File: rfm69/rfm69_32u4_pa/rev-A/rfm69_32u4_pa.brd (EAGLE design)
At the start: 69.8 x 69.8 mm, 125 parts, among them IC1 ATMEGA32U4-AU, IC2 74HC04D, IC3 MCP9700, SW1 HMC284AMS8G, SW1A TPSQTP10SQ, SW1B TPSQTP10SQ, SW2 HMC574AMS8E, SW2A TPSQTP10SQ, SW2B TPSQTP10SQ, Y1 8MHz

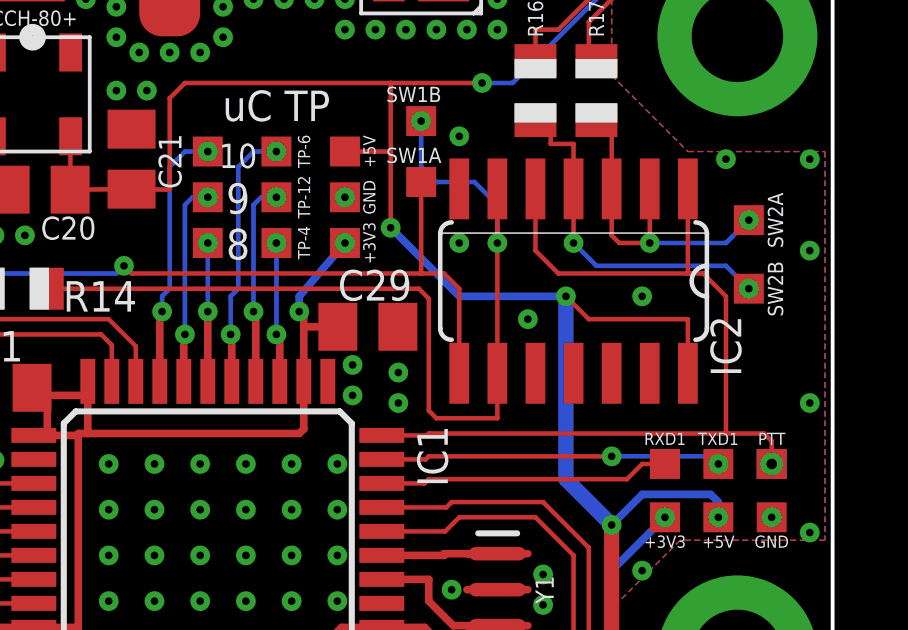
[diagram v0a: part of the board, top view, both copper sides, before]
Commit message: Changed PTT pin from physical pin 22 to physical pin 25 which is mapped to arduino digital pin 4.  This was done because there is no mapping of physical pin 22 to an arduino digital pin for the feather32u4.
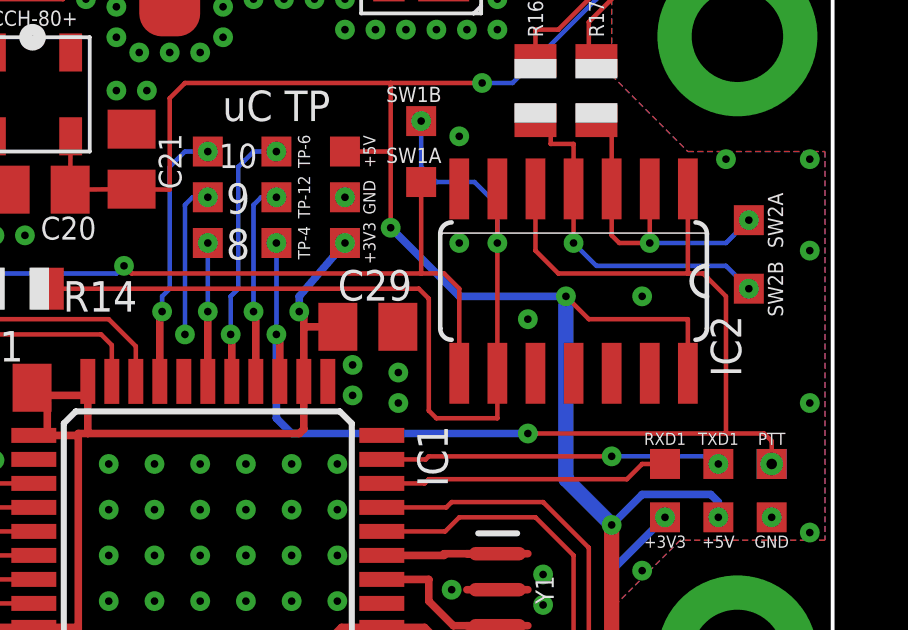
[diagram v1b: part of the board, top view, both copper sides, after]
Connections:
- removed net 22_TXRX_PTT: IC1.22, IC2.1, IC2.5, PTT.TP, PTT2.TP
- removed net 4: IC1.25, TP-4.TP
- new net 4_TXRX_PTT: IC1.25, IC2.1, IC2.5, PTT.TP, PTT2.TP, TP-4.TP
- new net NA: IC1.22
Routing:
- net 4_TXRX_PTT: track 0.00 -> 41.6 mm, vias 0 -> 4
- net 22_TXRX_PTT: track 30.3 -> 0.00 mm, vias 1 -> 0
- net 4: track 4.66 -> 0.00 mm, vias 2 -> 0
- net 9: track 6.77 -> 5.24 mm
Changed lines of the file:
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@@
 </signal>
 <signal name="9">
-<contactref element="IC1" pad="29"/>
 <contactref element="9" pad="TP"/>
 <via x="48.26" y="35.306" extent="1-16" drill="0.254"/>
-<wire x1="48.222" y1="33.74" x2="48.222" y2="35.268" width="0.254" layer="1"/>
 <wire x1="48.222" y1="35.268" x2="48.26" y2="35.306" width="0.254" layer="1"/>
 <via x="49.022" y="39.878" extent="1-16" drill="0.254"/>
@@
 <wire x1="48.26" y1="39.624" x2="48.514" y2="39.878" width="0.1524" layer="16"/>
 <wire x1="48.514" y1="39.878" x2="49.022" y2="39.878" width="0.1524" layer="16"/>
+<contactref element="IC1" pad="29"/>
+<wire x1="48.222" y1="33.74" x2="48.222" y2="35.268" width="0" layer="19" extent="1-1"/>
 </signal>
 <signal name="A3_RF_CS">
@@
 <wire x1="64.236" y1="12.218" x2="63.5" y2="12.446" width="0.1524" layer="1"/>
 <wire x1="63.5" y1="12.446" x2="57.658" y2="12.446" width="0.1524" layer="1"/>
-</signal>
-<signal name="4">
-<contactref element="IC1" pad="25"/>
-<via x="51.308" y="35.306" extent="1-16" drill="0.254"/>
-<wire x1="51.422" y1="33.74" x2="51.422" y2="35.192" width="0.254" layer="1"/>
-<wire x1="51.422" y1="35.192" x2="51.308" y2="35.306" width="0.254" layer="1"/>
-<contactref element="TP-4" pad="TP"/>
-<via x="51.308" y="38.354" extent="1-16" drill="0.254"/>
-<wire x1="51.308" y1="35.306" x2="51.308" y2="38.354" width="0.1524" layer="16"/>
 </signal>
 <signal name="10">
@@
 <wire x1="3.3161" y1="23.1441" x2="3.048" y2="23.384" width="0.508" layer="1"/>
 </signal>
-<signal name="22_TXRX_PTT">
-<contactref element="IC1" pad="22"/>
-<contactref element="IC2" pad="1"/>
-<contactref element="IC2" pad="5"/>
-<wire x1="65.024" y1="37.338" x2="60.706" y2="37.338" width="0.1524" layer="1"/>
-<wire x1="60.706" y1="37.338" x2="59.944" y2="38.1" width="0.1524" layer="1"/>
-<wire x1="59.944" y1="38.1" x2="59.944" y2="40.1574" width="0.1524" layer="1"/>
-<wire x1="65.532" y1="37.338" x2="66.294" y2="36.576" width="0.1524" layer="1"/>
-<wire x1="65.532" y1="37.338" x2="65.024" y2="37.338" width="0.1524" layer="1"/>
-<wire x1="65.024" y1="40.1574" x2="65.024" y2="37.338" width="0.1524" layer="1"/>
-<contactref element="PTT" pad="TP"/>
-<wire x1="66.294" y1="32.004" x2="66.294" y2="36.576" width="0.1524" layer="1"/>
-<wire x1="67.818" y1="30.988" x2="67.818" y2="31.75" width="0.1524" layer="1"/>
-<wire x1="67.818" y1="31.75" x2="67.564" y2="32.004" width="0.1524" layer="1"/>
-<wire x1="67.564" y1="32.004" x2="66.294" y2="32.004" width="0.1524" layer="1"/>
-<wire x1="54.822" y1="31.94" x2="56.324" y2="31.94" width="0.1524" layer="1"/>
-<wire x1="56.324" y1="31.94" x2="56.388" y2="32.004" width="0.1524" layer="1"/>
-<wire x1="56.388" y1="32.004" x2="66.294" y2="32.004" width="0.1524" layer="1"/>
-<contactref element="PTT2" pad="TP"/>
-<via x="67.818" y="30.988" extent="1-16" drill="0.35"/>
-</signal>
 <signal name="8_SD_CD">
 <contactref element="IC1" pad="8"/>
@@
 <wire x1="10.922" y1="59.96" x2="10.414" y2="59.96" width="0.1524" layer="1"/>
 </signal>
+<signal name="NA">
+<contactref element="IC1" pad="22"/>
+</signal>
+<signal name="4_TXRX_PTT">
+<contactref element="IC1" pad="25"/>
+<contactref element="PTT" pad="TP"/>
+<contactref element="PTT2" pad="TP"/>
+<via x="67.818" y="30.988" extent="1-16" drill="0.35"/>
+<via x="51.308" y="35.306" extent="1-16" drill="0.254"/>
+<wire x1="51.308" y1="35.306" x2="51.422" y2="35.192" width="0.254" layer="1"/>
+<contactref element="TP-4" pad="TP"/>
+<via x="51.308" y="38.354" extent="1-16" drill="0.254"/>
+<wire x1="51.308" y1="38.354" x2="51.308" y2="35.306" width="0.1524" layer="16"/>
+<wire x1="51.422" y1="33.74" x2="51.422" y2="35.192" width="0.254" layer="1"/>
+<wire x1="51.422" y1="35.192" x2="51.308" y2="35.306" width="0.254" layer="1"/>
+<wire x1="51.308" y1="35.306" x2="51.308" y2="32.512" width="0.254" layer="16"/>
+<wire x1="51.308" y1="32.512" x2="51.816" y2="32.004" width="0.254" layer="16"/>
+<wire x1="51.816" y1="32.004" x2="59.69" y2="32.004" width="0.254" layer="16"/>
+<via x="59.69" y="32.004" extent="1-16" drill="0.254"/>
+<contactref element="IC2" pad="5"/>
+<contactref element="IC2" pad="1"/>
+<wire x1="65.024" y1="37.338" x2="60.706" y2="37.338" width="0.1524" layer="1"/>
+<wire x1="59.944" y1="38.1" x2="60.706" y2="37.338" width="0.1524" layer="1"/>
+<wire x1="65.532" y1="37.338" x2="66.294" y2="36.576" width="0.1524" layer="1"/>
+<wire x1="65.532" y1="37.338" x2="65.024" y2="37.338" width="0.1524" layer="1"/>
+<wire x1="65.024" y1="40.1574" x2="65.024" y2="37.338" width="0.1524" layer="1"/>
+<wire x1="66.294" y1="32.004" x2="66.294" y2="36.576" width="0.1524" layer="1"/>
+<wire x1="67.818" y1="31.75" x2="67.564" y2="32.004" width="0.1524" layer="1"/>
+<wire x1="67.564" y1="32.004" x2="66.294" y2="32.004" width="0.1524" layer="1"/>
+<wire x1="59.944" y1="40.1574" x2="59.944" y2="38.1" width="0.1524" layer="1"/>
+<wire x1="59.69" y1="32.004" x2="66.294" y2="32.004" width="0.1524" layer="1"/>
+<wire x1="67.818" y1="30.988" x2="67.818" y2="31.75" width="0.1524" layer="1"/>
+</signal>
 </signals>

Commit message: Final updates.  Final Gerbers submitted for fabrication.
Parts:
- removed DIO0, DIO1, DIO2, DIO3, DIO4, DIO5, GND@1, PTT, PTT1, PTT2, TP-12, TP-4, TP-6, TP10, TP11, TP12, TP14, TP15, TXD1: TPSQTP10SQ, testpad:TP10SQ
- removed LED-ALT, PTT-HI, PTT-LO: (no value), adafruit:CHIPLED_0805
- removed TVS1: ESD8472, kj4qlp:X3DFN2
- added 12, 4, 6: TPSQTP10SQ, testpad:TP10SQ
- added C32: 1uF, rcl:C0805K
- added LED-PTT, LED-RX: (no value), adafruit:CHIPLED_0805
- added R19: 100, adafruit:R0805
- added R20: 100k, adafruit:R0805
- added R21: 10k, adafruit:R0805
- added T1, T2: (no value), transistor:SOT23-BEC
- added TP-GND, TP-VIN: TPSQTP20SQ, testpad:TP20SQ
- C14: value 1uF -> .01uF
- C21, C23, C25: value 10uF -> 22uF
- R11: value 10K -> 330
- R18: value 10K -> 3.3k
- TP3, TP7: value TPSQTP20SQ -> TPSQTP10SQ; device testpad:TP20SQ -> testpad:TP10SQ
- moved TP7 58.8 mm to (62.5, 21.1)
- moved TP1 54.8 mm to (60.7, 21.1)
- moved TP2 45.6 mm to (59.4, 42.9)
- moved TP5 43.2 mm to (58.9, 21.1)
- moved TP4 38.4 mm to (54.6, 38.4)
- moved TP6 26.0 mm to (54.6, 40.4)
- moved SJ5 17.1 mm to (10.2, 33.3), turned to 90 degrees
- moved C19 16.5 mm to (10.9, 38.1)
- moved C18 16.5 mm to (8.64, 38.1)
- moved C17 16.5 mm to (7.87, 41.9)
- moved R8 16.5 mm to (3.05, 40.9)
- moved VR2 16.5 mm to (5.84, 38.4)
- moved D1 15.2 mm to (14.0, 33.3), turned to 270 degrees
- moved USB 10.7 mm to (4.57, 24.1)
- moved R17 10.4 mm to (67.8, 52.1)
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- renumbered AIN0 to A0, AIN1 to A1, AIN2 to A2, AIN3 to A3
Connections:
- net RXD1 renamed 0_RX
- removed net 4_TXRX_PTT: IC1.25, IC2.1, IC2.5, PTT.TP, PTT2.TP, TP-4.TP
- removed net A0_RF_DIO0: DIO0.TP, IC1.36, RF1.14
- removed net N$27: PTT-LO.A, R18.2
- removed net N$5: PTT-HI.A, PTT-LO.C, PTT1.TP
- removed net TXD1: IC1.21, TXD1.TP
- new net 1_RF_DIO0: IC1.21, LED-RX.A, RF1.14
- new net 4_PTT: 4.TP, IC1.25, IC2.1, IC2.13, IC2.5, R20.1
- new net A0: IC1.36
- new net N$28: IC2.11, IC2.12, R21.2
- new net N$29: R18.2, R7.3
- new net N$30: T1.C, T2.B
- new net N$31: BT1.3, C20.1, C21.1, T2.C
- new net N$32: R19.2, T1.E
- new net N$34: R21.1, T1.B
- new net PTT_LED: IC2.10, LED-PTT.A, R18.1
- net +3V3: now also TP3.TP, TP4.TP; no longer R18.1, R7.1, TP11.TP, TP14.TP, TP2.TP
- net +5V: now also C32.1, T2.E, TP1.TP, TP2.TP; no longer BT1.3, C20.1, C21.1, TP10.TP, TP15.TP
- net 12: now also 12.TP; no longer TP-12.TP
- net 13_RF_DIO4: no longer DIO4.TP
- net 5_RF_DIO3: no longer DIO3.TP
- net 6: now also 6.TP; no longer TP-6.TP
- net A1_RF_DIO1: no longer DIO1.TP
- net A2_RF_DIO2: no longer DIO2.TP
- net A5_RF_DIO5: no longer DIO5.TP
- net ALERT: no longer LED-ALT.A
- net GND: now also C32.2, R19.1, R20.2, R7.1, TP-GND.TP; no longer GND@1.TP, R7.3, TP1.TP, TP12.TP, TP4.TP, TVS1.P$2
- net N$11: no longer TVS1.P$1
- net N$24: now also LED-RX.C; no longer LED-ALT.C
- net N$8: now also LED-PTT.C; no longer PTT-HI.C
- net VIN: now also TP-VIN.TP; no longer TP3.TP
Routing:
- net PTT_LED: track 0.00 -> 85.0 mm, vias 0 -> 8
- net 1_RF_DIO0: track 0.00 -> 75.1 mm, vias 0 -> 6
- net 4_PTT: track 0.00 -> 44.4 mm, vias 0 -> 5
- net 4_TXRX_PTT: track 41.6 -> 0.00 mm, vias 4 -> 0
- net A0_RF_DIO0: track 39.4 -> 0.00 mm, vias 2 -> 0
- net +3V3: track 272.4 -> 248.8 mm, vias 13 -> 10
- net N$31: track 0.00 -> 22.7 mm, vias 0 -> 2
- net 5_RF_DIO3: track 36.7 -> 16.8 mm, vias 2 -> 0
- net VBUS: track 81.3 -> 100.3 mm
- net 13_RF_DIO4: track 36.1 -> 17.9 mm, vias 2 -> 0
- net +12V: track 105.6 -> 88.6 mm
- net SW2A: track 11.1 -> 22.7 mm
- net TXD1: track 11.4 -> 0.00 mm, vias 2 -> 0
- net ALERT: track 10.6 -> 0.00 mm, vias 2 -> 0
- net N$25: track 17.0 -> 6.49 mm
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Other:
- board text added: "NET ID:"
- board text added: "NODE ID:"
- board text added: "PN: RFM69-32U4-RFFE, Rev A."
- board text removed: "PN:"
- board text removed: "REV:"
- board text removed: "RFM"
- board text removed: "SN:"
- board text removed: "TP"
- board text removed: "uC TP"
